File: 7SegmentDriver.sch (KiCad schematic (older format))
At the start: 6 parts

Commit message: [modified:] Display driving cleanup
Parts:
- removed IC?: TS5A23157DGSTG4, SOP50P490X110-10N, symbol TeKaDe:TS5A23157DGSTG4
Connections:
- net labels added: DecoderData, Digit1Cathode, Digit1CathodeSignal, Digit4Cathode, Digit4CathodeSignal, Digit5Cathode, Digit5CathodeSignal, DigitACathode, DigitACathodeSignal, DigitBCathode, DigitBCathodeSignal, DigitCathodes, GND, SegmentAnodes, SegmentDriverData
- net labels removed: DecoderExtraSwitch, DecoderS14, DecoderS15, Digit15Cathode, Digit15CathodeSignal, Digit16Cathode, Digit16CathodeSignal, Digit17Cathode, Digit17CathodeSignal, Digit18Cathode, Digit18CathodeSignal, Digit19Cathode, Digit19CathodeSignal, Digit20Cathode, Digit20CathodeSignal, Digit21Cathode, Digit21CathodeSignal, Earth
- wire segments 105 -> 89
- no-connect marks 6 -> 10
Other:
- moved on the sheet: U?

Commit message: [fix:] corrected CD4515 to CD4514
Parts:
- U?: value CD4515 -> CD4514; symbol TeKaDe:CD4515 -> TeKaDe:CD4514
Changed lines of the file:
@@
 Wire Wire Line
 	3500 2300 3250 2300
-$Comp
-L TeKaDe:CD4515 U?
-U 1 1 60FBCF10
-P 2850 2750
-AR Path="/60FBCF10" Ref="U?"  Part="1"
-AR Path="/60F87146/60FBCF10" Ref="U?"  Part="1"
-F 0 "U?" H 2850 3525 50  0000 C CNN
-F 1 "CD4515" H 2850 3434 50  0000 C CNN
-F 2 "Package_SO:SOIC-24W_7.5x15.4mm_P1.27mm" H 2850 3400 50  0001 C CNN
-F 3 "https://www.ti.com/lit/ds/symlink/cd4514b.pdf" H 2850 3400 50  0001 C CNN
-F 4 "good" H 2850 2750 50  0001 C CNN "Availability"
-	1    2850 2750
-	1    0    0    -1
-$EndComp
 Wire Wire Line
 	2200 3300 2450 3300
@@
 Wire Bus Line
 	1500 6100 1350 6100
-Wire Bus Line
-	4400 1900 4400 2400
-Wire Bus Line
-	1350 1900 1350 2300
-Wire Bus Line
-	1500 6100 1500 6450
-Wire Bus Line
-	5600 5350 5600 6150
-Wire Bus Line
-	9300 1050 9300 4950
 Text HLabel 2400 5950 0    50   Input ~ 0
 BrightnessRegulation
+$Comp
+L TeKaDe:CD4514 U?
+U 1 1 60FBCF10
+P 2850 2750
+AR Path="/60FBCF10" Ref="U?"  Part="1"
+AR Path="/60F87146/60FBCF10" Ref="U?"  Part="1"
+F 0 "U?" H 2850 3525 50  0000 C CNN
+F 1 "CD4514" H 2850 3434 50  0000 C CNN
+F 2 "Package_SO:SOIC-24W_7.5x15.4mm_P1.27mm" H 2850 3400 50  0001 C CNN
+F 3 "https://www.ti.com/lit/ds/symlink/cd4514b.pdf" H 2850 3400 50  0001 C CNN
+F 4 "good" H 2850 2750 50  0001 C CNN "Availability"
+	1    2850 2750
+	1    0    0    -1
+$EndComp
+Wire Bus Line
+	4400 1900 4400 2400
+Wire Bus Line
+	1350 1900 1350 2300
+Wire Bus Line
+	1500 6100 1500 6450
+Wire Bus Line
+	5600 5350 5600 6150
+Wire Bus Line
+	9300 1050 9300 4950
 $EndSCHEMATC

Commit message: - BT fertig, warten auf Rueckmeldung von Microchip - CM3 fast fertig - diverse Kleinigkeiten
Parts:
- gave numbers to parts that had none: 5
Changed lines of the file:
@@
 P 2200 1750
 AR Path="/60E3506C" Ref="#PWR?"  Part="1"
-AR Path="/60F87146/60E3506C" Ref="#PWR?"  Part="1"
-F 0 "#PWR?" H 2200 1600 50  0001 C CNN
+AR Path="/60F87146/60E3506C" Ref="#PWR0185"  Part="1"
+F 0 "#PWR0185" H 2200 1600 50  0001 C CNN
 F 1 "+5V" H 2215 1923 50  0000 C CNN
 F 2 "" H 2200 1750 50  0001 C CNN
@@
 	3500 2300 3500 3700
 $Comp
-L power:GND #PWR?
+L power:GND #PWR0190
 U 1 1 60DF5331
 P 3500 3700
-F 0 "#PWR?" H 3500 3450 50  0001 C CNN
+F 0 "#PWR0190" H 3500 3450 50  0001 C CNN
 F 1 "GND" H 3505 3527 50  0000 C CNN
 F 2 "" H 3500 3700 50  0001 C CNN
@@
 $EndComp
 $Comp
-L power:GND #PWR?
+L power:GND #PWR0189
 U 1 1 60DF4EA7
 P 2200 3700
-F 0 "#PWR?" H 2200 3450 50  0001 C CNN
+F 0 "#PWR0189" H 2200 3450 50  0001 C CNN
 F 1 "GND" H 2205 3527 50  0000 C CNN
 F 2 "" H 2200 3700 50  0001 C CNN
@@
 P 3500 1750
 AR Path="/60FBCEF3" Ref="#PWR?"  Part="1"
-AR Path="/60F87146/60FBCEF3" Ref="#PWR?"  Part="1"
-F 0 "#PWR?" H 3500 1600 50  0001 C CNN
+AR Path="/60F87146/60FBCEF3" Ref="#PWR0186"  Part="1"
+F 0 "#PWR0186" H 3500 1600 50  0001 C CNN
 F 1 "+5V" H 3515 1923 50  0000 C CNN
 F 2 "" H 3500 1750 50  0001 C CNN
@@
 NoConn ~ 8300 5150
 $Comp
-L power:GND #PWR?
+L power:GND #PWR0191
 U 1 1 60DCB09E
 P 7900 4050
-F 0 "#PWR?" H 7900 3800 50  0001 C CNN
+F 0 "#PWR0191" H 7900 3800 50  0001 C CNN
 F 1 "GND" H 7905 3877 50  0000 C CNN
 F 2 "" H 7900 4050 50  0001 C CNN
@@
 $EndComp
 $Comp
-L power:GND #PWR?
+L power:GND #PWR0194
 U 1 1 60DC7859
 P 7900 5850
-F 0 "#PWR?" H 7900 5600 50  0001 C CNN
+F 0 "#PWR0194" H 7900 5600 50  0001 C CNN
 F 1 "GND" H 7905 5677 50  0000 C CNN
 F 2 "" H 7900 5850 50  0001 C CNN
@@
 $EndComp
 $Comp
-L power:GND #PWR?
+L power:GND #PWR0187
 U 1 1 60DC3F48
 P 7900 2300
-F 0 "#PWR?" H 7900 2050 50  0001 C CNN
+F 0 "#PWR0187" H 7900 2050 50  0001 C CNN
 F 1 "GND" H 7905 2127 50  0000 C CNN
 F 2 "" H 7900 2300 50  0001 C CNN
@@
 P 8450 4600
 AR Path="/60FBCFA4" Ref="#PWR?"  Part="1"
-AR Path="/60F87146/60FBCFA4" Ref="#PWR?"  Part="1"
-F 0 "#PWR?" H 8450 4450 50  0001 C CNN
+AR Path="/60F87146/60FBCFA4" Ref="#PWR0192"  Part="1"
+F 0 "#PWR0192" H 8450 4450 50  0001 C CNN
 F 1 "+5V" H 8465 4773 50  0000 C CNN
 F 2 "" H 8450 4600 50  0001 C CNN
@@
 P 7900 5150
 AR Path="/60FBCF9E" Ref="U?"  Part="1"
-AR Path="/60F87146/60FBCF9E" Ref="U?"  Part="1"
-F 0 "U?" H 7900 5817 50  0000 C CNN
+AR Path="/60F87146/60FBCF9E" Ref="U18"  Part="1"
+F 0 "U18" H 7900 5817 50  0000 C CNN
 F 1 "ULN2003" H 7900 5726 50  0000 C CNN
 F 2 "" H 7950 4600 50  0001 L CNN
@@
 P 8450 2800
 AR Path="/60FBCF79" Ref="#PWR?"  Part="1"
-AR Path="/60F87146/60FBCF79" Ref="#PWR?"  Part="1"
-F 0 "#PWR?" H 8450 2650 50  0001 C CNN
+AR Path="/60F87146/60FBCF79" Ref="#PWR0188"  Part="1"
+F 0 "#PWR0188" H 8450 2650 50  0001 C CNN
 F 1 "+5V" H 8465 2973 50  0000 C CNN
 F 2 "" H 8450 2800 50  0001 C CNN
@@
 P 7900 3350
 AR Path="/60FBCF6C" Ref="U?"  Part="1"
-AR Path="/60F87146/60FBCF6C" Ref="U?"  Part="1"
-F 0 "U?" H 7900 4017 50  0000 C CNN
+AR Path="/60F87146/60FBCF6C" Ref="U17"  Part="1"
+F 0 "U17" H 7900 4017 50  0000 C CNN
 F 1 "ULN2003" H 7900 3926 50  0000 C CNN
 F 2 "" H 7950 2800 50  0001 L CNN
@@
 P 8450 1050
 AR Path="/60FBCF47" Ref="#PWR?"  Part="1"
-AR Path="/60F87146/60FBCF47" Ref="#PWR?"  Part="1"
-F 0 "#PWR?" H 8450 900 50  0001 C CNN
+AR Path="/60F87146/60FBCF47" Ref="#PWR0184"  Part="1"
+F 0 "#PWR0184" H 8450 900 50  0001 C CNN
 F 1 "+5V" H 8465 1223 50  0000 C CNN
 F 2 "" H 8450 1050 50  0001 C CNN
@@
 P 7900 1600
 AR Path="/60FBCF3A" Ref="U?"  Part="1"
-AR Path="/60F87146/60FBCF3A" Ref="U?"  Part="1"
-F 0 "U?" H 7900 2267 50  0000 C CNN
+AR Path="/60F87146/60FBCF3A" Ref="U15"  Part="1"
+F 0 "U15" H 7900 2267 50  0000 C CNN
 F 1 "ULN2003" H 7900 2176 50  0000 C CNN
 F 2 "" H 7950 1050 50  0001 L CNN
@@
 $EndComp
 $Comp
-L power:GND #PWR?
+L power:GND #PWR0195
 U 1 1 60DC32CA
 P 2650 7100
-F 0 "#PWR?" H 2650 6850 50  0001 C CNN
+F 0 "#PWR0195" H 2650 6850 50  0001 C CNN
 F 1 "GND" H 2655 6927 50  0000 C CNN
 F 2 "" H 2650 7100 50  0001 C CNN
@@
 P 2650 5400
 AR Path="/60FBCEC0" Ref="#PWR?"  Part="1"
-AR Path="/60F87146/60FBCEC0" Ref="#PWR?"  Part="1"
-F 0 "#PWR?" H 2650 5250 50  0001 C CNN
+AR Path="/60F87146/60FBCEC0" Ref="#PWR0193"  Part="1"
+F 0 "#PWR0193" H 2650 5250 50  0001 C CNN
 F 1 "+5V" H 2665 5573 50  0000 C CNN
 F 2 "" H 2650 5400 50  0001 C CNN
@@
 P 3600 6050
 AR Path="/60FBCEB3" Ref="U?"  Part="1"
-AR Path="/60F87146/60FBCEB3" Ref="U?"  Part="1"
-F 0 "U?" H 3600 6820 50  0000 C CNN
+AR Path="/60F87146/60FBCEB3" Ref="U19"  Part="1"
+F 0 "U19" H 3600 6820 50  0000 C CNN
 F 1 "CD4511" H 3600 6729 50  0000 C CNN
 F 2 "Package_SO:SOIC-24W_7.5x15.4mm_P1.27mm" H 3600 6050 50  0001 L BNN
@@
 P 2850 2750
 AR Path="/60FBCF10" Ref="U?"  Part="1"
-AR Path="/60F87146/60FBCF10" Ref="U?"  Part="1"
-F 0 "U?" H 2850 3525 50  0000 C CNN
+AR Path="/60F87146/60FBCF10" Ref="U16"  Part="1"
+F 0 "U16" H 2850 3525 50  0000 C CNN
 F 1 "CD4514" H 2850 3434 50  0000 C CNN
 F 2 "Package_SO:SOIC-24W_7.5x15.4mm_P1.27mm" H 2850 3400 50  0001 C CNN

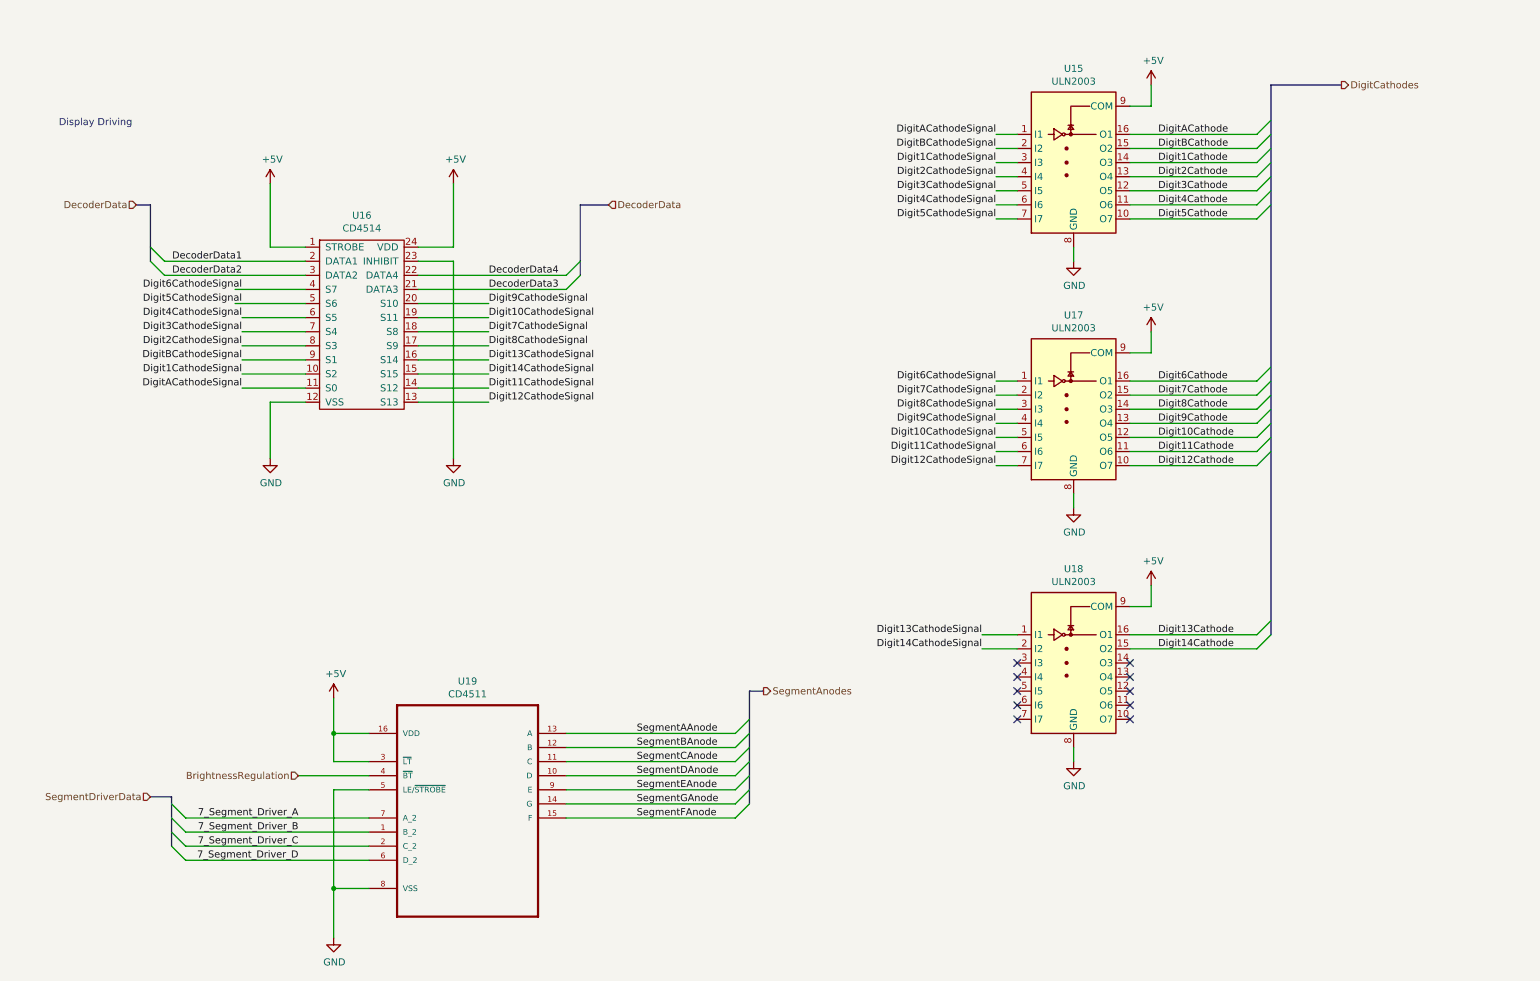
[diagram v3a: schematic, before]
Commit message: - CM3 durch CM4 ersetzt - Spannungsregler für 3,3 und 1,8V entfernt, da nun von CM4 erzeugt - RTC IC getauscht
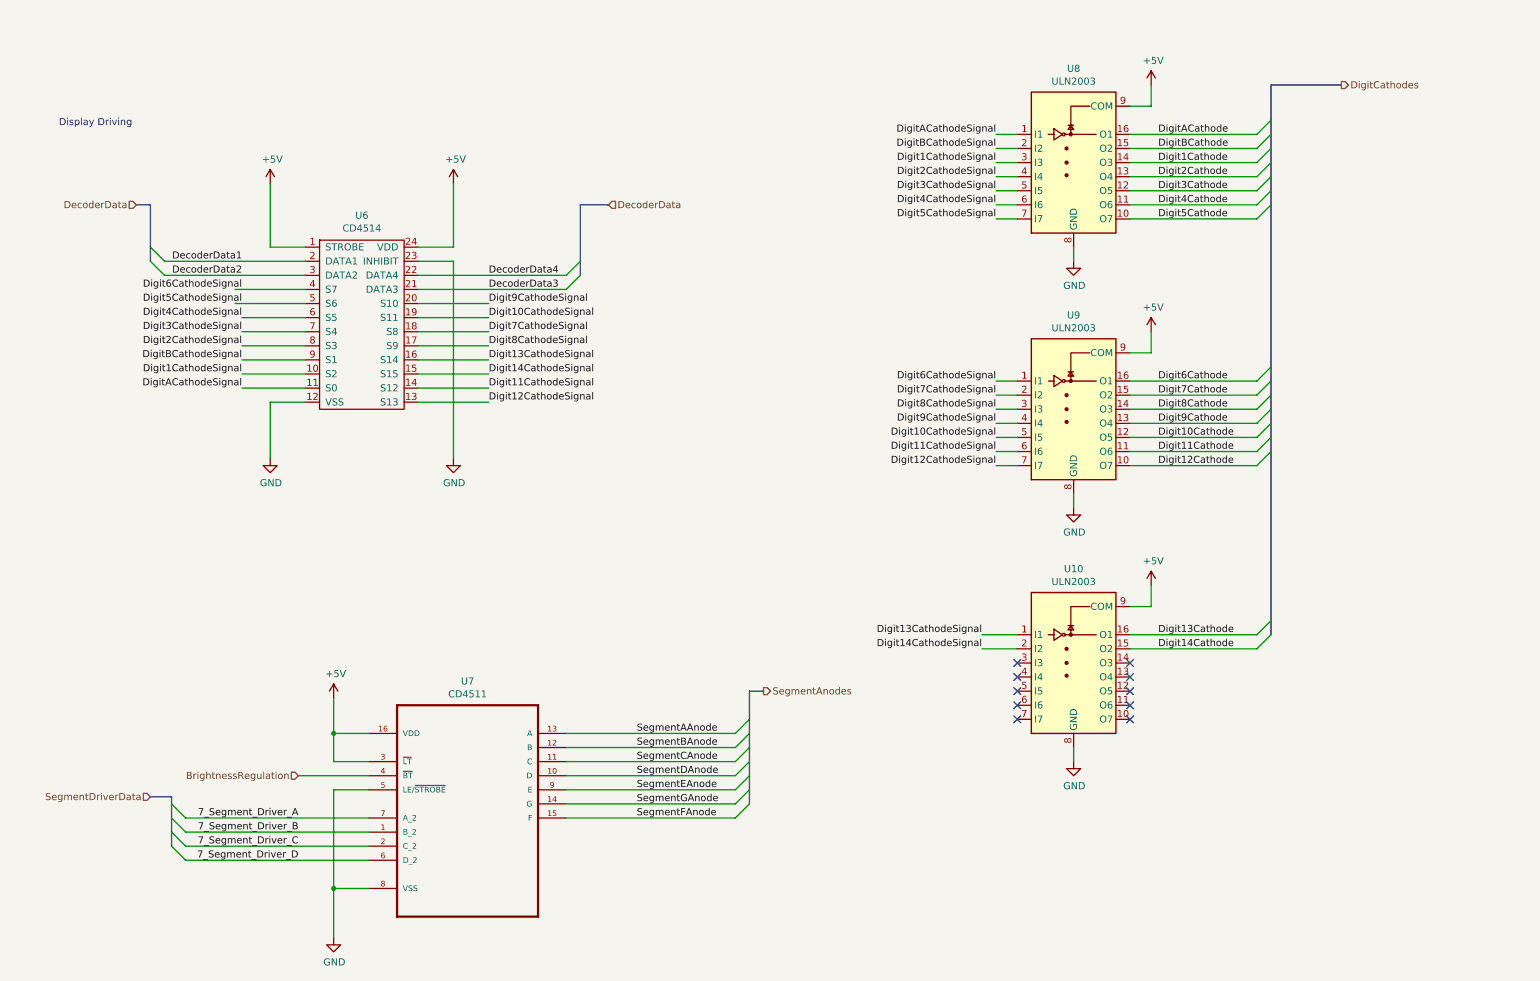
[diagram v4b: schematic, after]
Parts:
- renumbered U18 to U10, U16 to U6, U19 to U7, U15 to U8, U17 to U9
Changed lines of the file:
@@
 $Descr A4 11693 8268
 encoding utf-8
-Sheet 7 7
+Sheet 7 8
 Title ""
 Date ""
@@
 P 2200 1750
 AR Path="/60E3506C" Ref="#PWR?"  Part="1"
-AR Path="/60F87146/60E3506C" Ref="#PWR0185"  Part="1"
-F 0 "#PWR0185" H 2200 1600 50  0001 C CNN
+AR Path="/60F87146/60E3506C" Ref="#PWR086"  Part="1"
+F 0 "#PWR086" H 2200 1600 50  0001 C CNN
 F 1 "+5V" H 2215 1923 50  0000 C CNN
 F 2 "" H 2200 1750 50  0001 C CNN
@@
 	3500 2300 3500 3700
 $Comp
-L power:GND #PWR0190
+L power:GND #PWR091
 U 1 1 60DF5331
 P 3500 3700
-F 0 "#PWR0190" H 3500 3450 50  0001 C CNN
+F 0 "#PWR091" H 3500 3450 50  0001 C CNN
 F 1 "GND" H 3505 3527 50  0000 C CNN
 F 2 "" H 3500 3700 50  0001 C CNN
@@
 $EndComp
 $Comp
-L power:GND #PWR0189
+L power:GND #PWR087
 U 1 1 60DF4EA7
 P 2200 3700
-F 0 "#PWR0189" H 2200 3450 50  0001 C CNN
+F 0 "#PWR087" H 2200 3450 50  0001 C CNN
 F 1 "GND" H 2205 3527 50  0000 C CNN
 F 2 "" H 2200 3700 50  0001 C CNN
@@
 P 3500 1750
 AR Path="/60FBCEF3" Ref="#PWR?"  Part="1"
-AR Path="/60F87146/60FBCEF3" Ref="#PWR0186"  Part="1"
-F 0 "#PWR0186" H 3500 1600 50  0001 C CNN
+AR Path="/60F87146/60FBCEF3" Ref="#PWR090"  Part="1"
+F 0 "#PWR090" H 3500 1600 50  0001 C CNN
 F 1 "+5V" H 3515 1923 50  0000 C CNN
 F 2 "" H 3500 1750 50  0001 C CNN
@@
 NoConn ~ 8300 5150
 $Comp
-L power:GND #PWR0191
+L power:GND #PWR093
 U 1 1 60DCB09E
 P 7900 4050
-F 0 "#PWR0191" H 7900 3800 50  0001 C CNN
+F 0 "#PWR093" H 7900 3800 50  0001 C CNN
 F 1 "GND" H 7905 3877 50  0000 C CNN
 F 2 "" H 7900 4050 50  0001 C CNN
@@
 $EndComp
 $Comp
-L power:GND #PWR0194
+L power:GND #PWR094
 U 1 1 60DC7859
 P 7900 5850
-F 0 "#PWR0194" H 7900 5600 50  0001 C CNN
+F 0 "#PWR094" H 7900 5600 50  0001 C CNN
 F 1 "GND" H 7905 5677 50  0000 C CNN
 F 2 "" H 7900 5850 50  0001 C CNN
@@
 $EndComp
 $Comp
-L power:GND #PWR0187
+L power:GND #PWR092
 U 1 1 60DC3F48
 P 7900 2300
-F 0 "#PWR0187" H 7900 2050 50  0001 C CNN
+F 0 "#PWR092" H 7900 2050 50  0001 C CNN
 F 1 "GND" H 7905 2127 50  0000 C CNN
 F 2 "" H 7900 2300 50  0001 C CNN
@@
 P 8450 4600
 AR Path="/60FBCFA4" Ref="#PWR?"  Part="1"
-AR Path="/60F87146/60FBCFA4" Ref="#PWR0192"  Part="1"
-F 0 "#PWR0192" H 8450 4450 50  0001 C CNN
+AR Path="/60F87146/60FBCFA4" Ref="#PWR097"  Part="1"
+F 0 "#PWR097" H 8450 4450 50  0001 C CNN
 F 1 "+5V" H 8465 4773 50  0000 C CNN
 F 2 "" H 8450 4600 50  0001 C CNN
@@
 P 7900 5150
 AR Path="/60FBCF9E" Ref="U?"  Part="1"
-AR Path="/60F87146/60FBCF9E" Ref="U18"  Part="1"
-F 0 "U18" H 7900 5817 50  0000 C CNN
+AR Path="/60F87146/60FBCF9E" Ref="U10"  Part="1"
+F 0 "U10" H 7900 5817 50  0000 C CNN
 F 1 "ULN2003" H 7900 5726 50  0000 C CNN
 F 2 "" H 7950 4600 50  0001 L CNN
@@
 P 8450 2800
 AR Path="/60FBCF79" Ref="#PWR?"  Part="1"
-AR Path="/60F87146/60FBCF79" Ref="#PWR0188"  Part="1"
-F 0 "#PWR0188" H 8450 2650 50  0001 C CNN
+AR Path="/60F87146/60FBCF79" Ref="#PWR096"  Part="1"
+F 0 "#PWR096" H 8450 2650 50  0001 C CNN
 F 1 "+5V" H 8465 2973 50  0000 C CNN
 F 2 "" H 8450 2800 50  0001 C CNN
@@
 P 7900 3350
 AR Path="/60FBCF6C" Ref="U?"  Part="1"
-AR Path="/60F87146/60FBCF6C" Ref="U17"  Part="1"
-F 0 "U17" H 7900 4017 50  0000 C CNN
+AR Path="/60F87146/60FBCF6C" Ref="U9"  Part="1"
+F 0 "U9" H 7900 4017 50  0000 C CNN
 F 1 "ULN2003" H 7900 3926 50  0000 C CNN
 F 2 "" H 7950 2800 50  0001 L CNN
@@
 P 8450 1050
 AR Path="/60FBCF47" Ref="#PWR?"  Part="1"
-AR Path="/60F87146/60FBCF47" Ref="#PWR0184"  Part="1"
-F 0 "#PWR0184" H 8450 900 50  0001 C CNN
+AR Path="/60F87146/60FBCF47" Ref="#PWR095"  Part="1"
+F 0 "#PWR095" H 8450 900 50  0001 C CNN
 F 1 "+5V" H 8465 1223 50  0000 C CNN
 F 2 "" H 8450 1050 50  0001 C CNN
@@
 P 7900 1600
 AR Path="/60FBCF3A" Ref="U?"  Part="1"
-AR Path="/60F87146/60FBCF3A" Ref="U15"  Part="1"
-F 0 "U15" H 7900 2267 50  0000 C CNN
+AR Path="/60F87146/60FBCF3A" Ref="U8"  Part="1"
+F 0 "U8" H 7900 2267 50  0000 C CNN
 F 1 "ULN2003" H 7900 2176 50  0000 C CNN
 F 2 "" H 7950 1050 50  0001 L CNN
@@
 $EndComp
 $Comp
-L power:GND #PWR0195
+L power:GND #PWR089
 U 1 1 60DC32CA
 P 2650 7100
-F 0 "#PWR0195" H 2650 6850 50  0001 C CNN
+F 0 "#PWR089" H 2650 6850 50  0001 C CNN
 F 1 "GND" H 2655 6927 50  0000 C CNN
 F 2 "" H 2650 7100 50  0001 C CNN
@@
 P 2650 5400
 AR Path="/60FBCEC0" Ref="#PWR?"  Part="1"
-AR Path="/60F87146/60FBCEC0" Ref="#PWR0193"  Part="1"
-F 0 "#PWR0193" H 2650 5250 50  0001 C CNN
+AR Path="/60F87146/60FBCEC0" Ref="#PWR088"  Part="1"
+F 0 "#PWR088" H 2650 5250 50  0001 C CNN
 F 1 "+5V" H 2665 5573 50  0000 C CNN
 F 2 "" H 2650 5400 50  0001 C CNN
@@
 P 3600 6050
 AR Path="/60FBCEB3" Ref="U?"  Part="1"
-AR Path="/60F87146/60FBCEB3" Ref="U19"  Part="1"
-F 0 "U19" H 3600 6820 50  0000 C CNN
+AR Path="/60F87146/60FBCEB3" Ref="U7"  Part="1"
+F 0 "U7" H 3600 6820 50  0000 C CNN
 F 1 "CD4511" H 3600 6729 50  0000 C CNN
 F 2 "Package_SO:SOIC-24W_7.5x15.4mm_P1.27mm" H 3600 6050 50  0001 L BNN
@@
 P 2850 2750
 AR Path="/60FBCF10" Ref="U?"  Part="1"
-AR Path="/60F87146/60FBCF10" Ref="U16"  Part="1"
-F 0 "U16" H 2850 3525 50  0000 C CNN
+AR Path="/60F87146/60FBCF10" Ref="U6"  Part="1"
+F 0 "U6" H 2850 3525 50  0000 C CNN
 F 1 "CD4514" H 2850 3434 50  0000 C CNN
 F 2 "Package_SO:SOIC-24W_7.5x15.4mm_P1.27mm" H 2850 3400 50  0001 C CNN

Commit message: - Zwischenstand Display Driving
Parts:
- removed U10, U8, U9: ULN2003, symbol Transistor_Array:ULN2003
- removed U6: CD4514, Package_SO:SOIC-24W_7.5x15.4mm_P1.27mm, symbol TeKaDe:CD4514
- removed U7: CD4511, Package_SO:SOIC-24W_7.5x15.4mm_P1.27mm, symbol TeKaDe:CD4511BE
- added C? (x2): 100n/10V/X7R, Resistor_SMD:R_0603_1608Metric, symbol Device:C
- added J?: Conn_02x15_Odd_Even, Connector_PinSocket_2.54mm:PinSocket_2x15_P2.54mm_Vertical, symbol Connector_Generic:Conn_02x15_Odd_Even
- added U? (x3): ULN2003, symbol Transistor_Array:ULN2003
- added U?: CD4511, Package_SO:SOIC-24W_7.5x15.4mm_P1.27mm, symbol TeKaDe:CD4511BE
- added U?: CD4514, Package_SO:SOIC-24W_7.5x15.4mm_P1.27mm, symbol TeKaDe:CD4514
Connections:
- net +5V: now also C?.1, C?.1, J?.29 (Pin_29), U?.1 (STROBE), U?.16 (VDD), U?.24 (VDD), U?.3 (~LT), U?.9 (COM), U?.9 (COM), U?.9 (COM)
- net BrightnessRegulation: now also U?.4 (~BT)
- net Digit10Cathode: now also J?.13 (Pin_13), U?.12 (O5)
- net Digit10CathodeSignal: now also U?.19 (S11), U?.5 (I5)
- net Digit11Cathode: now also J?.16 (Pin_16), U?.11 (O6)
- net Digit11CathodeSignal: now also U?.14 (S12), U?.6 (I6)
- net Digit12Cathode: now also J?.15 (Pin_15), U?.10 (O7)
- net Digit12CathodeSignal: now also U?.13 (S13), U?.7 (I7)
- net Digit13Cathode: now also J?.18 (Pin_18), U?.16 (O1)
- net Digit13CathodeSignal: now also U?.1 (I1), U?.16 (S14)
- net Digit14Cathode: now also J?.9 (Pin_9), U?.15 (O2)
- net Digit14CathodeSignal: now also U?.15 (S15), U?.2 (I2)
- net Digit1Cathode: now also J?.21 (Pin_21), U?.14 (O3)
- net Digit1CathodeSignal: now also U?.10 (S2), U?.3 (I3)
- net Digit2Cathode: now also J?.22 (Pin_22), U?.13 (O4)
- net Digit2CathodeSignal: now also U?.4 (I4), U?.8 (S3)
- net Digit3Cathode: now also J?.23 (Pin_23), U?.12 (O5)
- net Digit3CathodeSignal: now also U?.5 (I5), U?.7 (S4)
- net Digit4Cathode: now also J?.24 (Pin_24), U?.11 (O6)
- net Digit4CathodeSignal: now also U?.6 (I6), U?.6 (S5)
- net Digit5Cathode: now also J?.25 (Pin_25), U?.10 (O7)
- net Digit5CathodeSignal: now also U?.5 (S6), U?.7 (I7)
- net Digit6Cathode: now also J?.17 (Pin_17), U?.16 (O1)
- net Digit6CathodeSignal: now also U?.1 (I1), U?.4 (S7)
- net Digit7Cathode: now also J?.12 (Pin_12), U?.15 (O2)
- net Digit7CathodeSignal: now also U?.18 (S8), U?.2 (I2)
- net Digit8Cathode: now also J?.11 (Pin_11), U?.14 (O3)
- net Digit8CathodeSignal: now also U?.17 (S9), U?.3 (I3)
- net Digit9Cathode: now also J?.14 (Pin_14), U?.13 (O4)
- net Digit9CathodeSignal: now also U?.20 (S10), U?.4 (I4)
- net DigitACathode: now also J?.19 (Pin_19), U?.16 (O1)
- net DigitACathodeSignal: now also U?.1 (I1), U?.11 (S0)
- net DigitBCathode: now also J?.20 (Pin_20), U?.15 (O2)
- net DigitBCathodeSignal: now also U?.2 (I2), U?.9 (S1)
- net GND: now also C?.2, C?.2, J?.27 (Pin_27), U?.12 (VSS), U?.23 (INHIBIT), U?.5 (LE/~STROBE), U?.8 (GND), U?.8 (GND), U?.8 (GND), U?.8 (VSS)
- net SegmentAAnode: now also J?.4 (Pin_4), U?.13 (A)
- net SegmentBAnode: now also J?.3 (Pin_3), U?.12 (B)
- net SegmentCAnode: now also J?.8 (Pin_8), U?.11 (C)
- net SegmentDAnode: now also J?.6 (Pin_6), U?.10 (D)
- net SegmentEAnode: now also J?.2 (Pin_2), U?.9 (E)
- net SegmentFAnode: now also J?.1 (Pin_1), U?.15 (F)
- net SegmentGAnode: now also J?.5 (Pin_5), U?.14 (G)
- new net 7Seg_Decoder_D1: U?.2 (DATA1)
- new net 7Seg_Decoder_D2: U?.3 (DATA2)
- new net 7Seg_Decoder_D3: U?.21 (DATA3)
- new net 7Seg_Decoder_D4: U?.22 (DATA4)
- new net 7Seg_Driver_A: U?.7 (A_2)
- new net 7Seg_Driver_B: U?.1 (B_2)
- new net 7Seg_Driver_C: U?.2 (C_2)
- new net 7Seg_Driver_D: U?.6 (D_2)
- no-connect marks 10 -> 15
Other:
- note added: "Änderungen:\n- Bypass C für CD4511 / CD4514"
- note removed: "Display Driving"
